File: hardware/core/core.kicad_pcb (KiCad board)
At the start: 2 copper layers, 256.5 x 129.5 mm, 86 parts, among them J1 9V_IN, J2 MIDI IN, J3 MIDI OUT 1, J4 MIDI OUT 2, J5 MIDI OUT 3, J6 MIDI OUT 4, J7 LCD, J8 USB_C_Receptacle_USB2.0_16P, SW1 FS, SW10 BOOT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

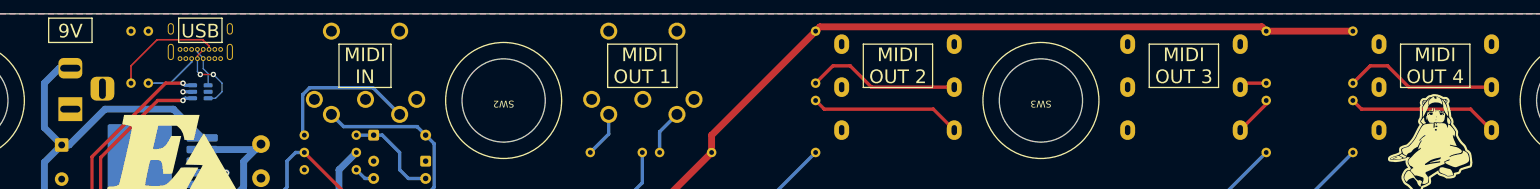
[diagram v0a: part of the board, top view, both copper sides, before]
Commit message: Adjust connector positions and reroute nearby traces
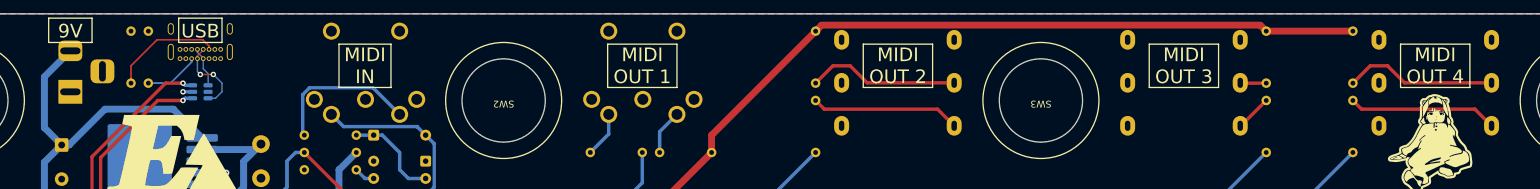
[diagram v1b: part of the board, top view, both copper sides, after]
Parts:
- moved J1 2.54 mm to (100.3, 99.1)
- moved J4 0.64 mm to (221.6, 97.7)
- moved J5 0.64 mm to (263.5, 97.7)
- moved J6 0.64 mm to (300.4, 97.7)
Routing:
- net +9V: track 50.9 -> 52.5 mm
- net Net-(J5-PadT): track 5.92 -> 5.35 mm
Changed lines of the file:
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@@
 	(footprint "Connector_BarrelJack:BarrelJack_Horizontal"
 		(layer "B.Cu")
-		(at 100.33 101.6 -90)
+		(at 100.33 99.06 -90)
 		(descr "DC Barrel Jack")
 		(tags "Power Jack")
@@
 	(footprint "midilord:CK635-006"
 		(layer "B.Cu")
-		(at 263.53 98.375 180)
+		(at 263.53 97.74 180)
 		(property "Reference" "J5"
 			(at 0 0.5 0)
@@
 	(footprint "midilord:CK635-006"
 		(layer "B.Cu")
-		(at 221.62 98.375 180)
+		(at 221.61 97.74 180)
 		(property "Reference" "J4"
 			(at 0 0.5 0)
@@
 	(footprint "midilord:CK635-006"
 		(layer "B.Cu")
-		(at 300.36 98.375 180)
+		(at 300.36 97.74 180)
 		(property "Reference" "J6"
 			(at 0 0.5 0)
@@
 	)
 	(segment
-		(start 100.33 95.6)
-		(end 98.71 95.6)
+		(start 96.52 104.312323)
+		(end 96.52 96.87)
 		(width 1)
 		(layer "B.Cu")
@@
 	)
 	(segment
-		(start 96.52 97.79)
+		(start 99.06 106.852323)
 		(end 96.52 104.312323)
 		(width 1)
@@
 	)
 	(segment
-		(start 96.52 104.312323)
-		(end 99.06 106.852323)
+		(start 105.41 101.6)
+		(end 100.157677 106.852323)
 		(width 1)
 		(layer "B.Cu")
@@
 	)
 	(segment
-		(start 105.41 101.6)
-		(end 100.157677 106.852323)
+		(start 96.52 96.87)
+		(end 100.33 93.06)
 		(width 1)
 		(layer "B.Cu")
@@
 	)
 	(segment
-		(start 98.71 95.6)
-		(end 96.52 97.79)
-		(width 1)
-		(layer "B.Cu")
-		(net 2)
-	)
-	(segment
 		(start 119.64 105.82)
 		(end 115.42 101.6)
@@
 	)
 	(segment
-		(start 272.365 97.79)
-		(end 271.78 98.375)
+		(start 271.83 97.79)
+		(end 271.78 97.74)
 		(width 0.5)
 		(layer "F.Cu")
@@
 	(segment
 		(start 275.59 97.79)
-		(end 272.365 97.79)
+		(end 271.83 97.79)
 		(width 0.5)
 		(layer "F.Cu")
@@
 	)
 	(segment
-		(start 275.59 100.865)
-		(end 271.78 104.675)
+		(start 275.59 100.33)
+		(end 271.88 104.04)
 		(width 0.5)
 		(layer "F.Cu")
@@
 	)
 	(segment
-		(start 275.59 100.33)
-		(end 275.59 100.865)
+		(start 271.88 104.04)
+		(end 271.78 104.04)
 		(width 0.5)
 		(layer "F.Cu")
@@
 	)
 	(segment
-		(start 288.29 97.79)
-		(end 290.83 95.25)
+		(start 293.37 95.25)
+		(end 295.86 97.74)
 		(width 0.5)
 		(layer "F.Cu")
@@
 	)
 	(segment
-		(start 296.495 98.375)
-		(end 308.61 98.375)
+		(start 288.29 97.79)
+		(end 290.83 95.25)
 		(width 0.5)
 		(layer "F.Cu")
@@
 	)
 	(segment
-		(start 293.37 95.25)
-		(end 296.495 98.375)
+		(start 295.86 97.74)
+		(end 308.61 97.74)
 		(width 0.5)
 		(layer "F.Cu")
@@
 	)
 	(segment
-		(start 288.29 100.33)
-		(end 289.56 101.6)
+		(start 289.56 101.6)
+		(end 306.17 101.6)
 		(width 0.5)
 		(layer "F.Cu")
@@
 	)
 	(segment
-		(start 289.56 101.6)
-		(end 305.535 101.6)
+		(start 306.17 101.6)
+		(end 308.61 104.04)
 		(width 0.5)
 		(layer "F.Cu")
@@
 	)
 	(segment
-		(start 305.535 101.6)
-		(end 308.61 104.675)
+		(start 288.29 100.33)
+		(end 289.56 101.6)
 		(width 0.5)
 		(layer "F.Cu")
@@
 	)
 	(segment
-		(start 146.05 120.65)
-		(end 142.24 124.46)
+		(start 210.431 89.289)
+		(end 209.55 90.17)
 		(width 1)
 		(layer "F.Cu")
@@
 	)
 	(segment
-		(start 209.55 90.17)
-		(end 194.31 105.41)
+		(start 146.05 120.65)
+		(end 142.24 124.46)
 		(width 1)
 		(layer "F.Cu")
@@
 	)
 	(segment
-		(start 210.185 89.535)
-		(end 209.55 90.17)
+		(start 209.55 90.17)
+		(end 194.31 105.41)
 		(width 1)
 		(layer "F.Cu")
@@
 	)
 	(segment
-		(start 274.955 89.535)
-		(end 210.185 89.535)
+		(start 146.05 120.65)
+		(end 181.61 120.65)
 		(width 1)
 		(layer "F.Cu")
@@
 	)
 	(segment
-		(start 146.05 120.65)
-		(end 181.61 120.65)
+		(start 274.709 89.289)
+		(end 210.431 89.289)
 		(width 1)
 		(layer "F.Cu")
@@
 	(segment
 		(start 275.59 90.17)
-		(end 274.955 89.535)
+		(end 274.709 89.289)
 		(width 1)
 		(layer "F.Cu")
@@
 	)
 	(segment
-		(start 209.55 100.33)
-		(end 210.82 101.6)
+		(start 227.42 101.6)
+		(end 229.86 104.04)
 		(width 0.5)
 		(layer "F.Cu")
@@
 	)
 	(segment
-		(start 210.82 101.6)
-		(end 226.795 101.6)
+		(start 209.55 100.33)
+		(end 210.82 101.6)
 		(width 0.5)
 		(layer "F.Cu")
@@
 	)
 	(segment
-		(start 226.795 101.6)
-		(end 229.87 104.675)
+		(start 210.82 101.6)
+		(end 227.42 101.6)
 		(width 0.5)
 		(layer "F.Cu")
@@
 	)
 	(segment
-		(start 217.755 98.375)
-		(end 229.87 98.375)
+		(start 212.09 95.25)
+		(end 214.63 95.25)
 		(width 0.5)
 		(layer "F.Cu")
@@
 	)
 	(segment
-		(start 209.55 97.79)
-		(end 212.09 95.25)
+		(start 214.63 95.25)
+		(end 217.12 97.74)
 		(width 0.5)
 		(layer "F.Cu")
@@
 	)
 	(segment
-		(start 214.63 95.25)
-		(end 217.755 98.375)
+		(start 209.55 97.79)
+		(end 212.09 95.25)
 		(width 0.5)
 		(layer "F.Cu")
@@
 	)
 	(segment
-		(start 212.09 95.25)
-		(end 214.63 95.25)
+		(start 217.12 97.74)
+		(end 229.86 97.74)
 		(width 0.5)
 		(layer "F.Cu")

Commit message: Move footswitch silkscreen circle to Dwgs.User layer
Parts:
- removed the G*** at (300.4, 106.7)
- moved G*** 117.8 mm to (203.2, 189.2)
- moved J1 0.64 mm to (100.3, 98.4)
- moved J2 0.18 mm to (143.5, 95.2)
- moved J3 0.18 mm to (184.2, 95.2)
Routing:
- net +9V: track 52.5 -> 53.1 mm
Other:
- board text added: "midiLORD"
- board text removed: "midilord"

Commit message: Add event system, switch matrix, MIDI outputs, and LED helpers
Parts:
- removed the G*** at (123.9, 204.3)
- removed J6: MIDI OUT 4, midilord:CK635-006
- added D19: 1N4148, Diode_THT:D_T-1_P5.08mm_Horizontal, B.Cu at (310.5, 140.3)
- added D20: 1N4148, Diode_THT:D_T-1_P5.08mm_Horizontal, B.Cu at (302.3, 140.3)
- added J9: MIDI OUT 2/3, midilord:CK635-037, B.Cu at (254.6, 97.8)
- added JP9: CONTRAST, Jumper:SolderJumper-3_P1.3mm_Open_RoundedPad1.0x1.5mm, F.Cu at (97.1, 167.6)
- added K1: G5V-1, Relay_THT:Relay_SPDT_Omron_G5V-1, B.Cu at (310.5, 137.2)
- added K2: G5V-1, Relay_THT:Relay_SPDT_Omron_G5V-1, B.Cu at (302.3, 137.2)
- added Q1: 2N3906, Package_TO_SOT_THT:TO-92_Inline_Wide, B.Cu at (217.2, 109.9)
- added Q2: 2N3906, Package_TO_SOT_THT:TO-92_Inline_Wide, B.Cu at (252.1, 115.6)
- added Q3: 2N3904, Package_TO_SOT_THT:TO-92_Inline_Wide, B.Cu at (310.5, 144.1)
- added Q4: 2N3904, Package_TO_SOT_THT:TO-92_Inline_Wide, B.Cu at (302.3, 144.1)
- added R17: 4.7K, Resistor_THT:R_Axial_DIN0204_L3.6mm_D1.6mm_P7.62mm_Horizontal, B.Cu at (205.7, 108.6)
- added R18: 4.7K, Resistor_THT:R_Axial_DIN0204_L3.6mm_D1.6mm_P7.62mm_Horizontal, B.Cu at (250.8, 120.7)
- D11, D12, D13, D14, D15, D16, D17, D18: footprint Diode_THT:D_DO-35_SOD27_P7.62mm_Horizontal -> Diode_THT:D_T-1_P5.08mm_Horizontal
- J4: value MIDI OUT 2 -> SWITCHES OUT; footprint midilord:CK635-006 -> midilord:CK635-037
- J5: value MIDI OUT 3 -> EXP/AUX IN; footprint midilord:CK635-006 -> midilord:CK635-037
- R10: value 33R -> 4.7K
- R3, R5, R7: value 10R -> 220R
- R4, R6, R8: value 33R -> 220R
- R9: value 10R -> 4.7K
- moved D10 234.5 mm to (306.1, 186.7), turned to 180 degrees
- moved D7 228.3 mm to (100.3, 186.7), turned to 180 degrees
- moved C15 223.4 mm to (293.4, 182.9)
- moved C12 205.1 mm to (113.0, 183.0), turned to -90 degrees
- moved D9 103.0 mm to (237.5, 186.7), turned to 180 degrees
- moved D8 98.3 mm to (168.9, 186.7), turned to 180 degrees
- moved C13 77.2 mm to (181.6, 183.0), turned to -90 degrees
- moved C14 77.2 mm to (224.8, 182.9), turned to -90 degrees
- moved D6 71.0 mm to (306.1, 118.1)
- moved D3 69.6 mm to (100.3, 118.1)
- moved D5 69.1 mm to (237.5, 118.1)
- moved D4 68.6 mm to (168.9, 118.1)
- moved U3 68.1 mm to (134.6, 204.5), turned to 0 degrees
- moved J4 67.3 mm to (288.9, 97.8)
- moved C11 66.7 mm to (293.4, 121.8)
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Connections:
- J7 pad 16: unconnected-(J7-Pin_16-Pad16) -> Net-(J7-Pin_16)
- R10 pad 1: MIDI_OUT4 -> SW_OUT2
- R3 pad 1: +3.3V -> +5V
- R4 pad 1: MIDI_OUT1 -> Net-(Q1-E)
- R5 pad 1: +3.3V -> +5V
- R5 pad 2: Net-(J4-PadR) -> Net-(J9-2R)
- R6 pad 1: MIDI_OUT2 -> Net-(Q2-E)
- R6 pad 2: Net-(J4-PadT) -> Net-(J9-T)
- R7 pad 1: +3.3V -> Net-(J9-R)
- R7 pad 2: Net-(J5-PadR) -> +5V
- R8 pad 1: MIDI_OUT3 -> Net-(Q2-E)
- R8 pad 2: Net-(J5-PadT) -> Net-(J9-2T)
- R9 pad 1: +3.3V -> SW_OUT1
- RV1 pad 3: GND -> Net-(JP9-C)
- U3 pad 10: DB6 -> RS
- U3 pad 11: DB5 -> E2
- U3 pad 12: DB4 -> SW_OUT3
- U3 pad 17: unconnected-(U3-IO9-Pad17) -> MIDI_IN
- U3 pad 18: unconnected-(U3-IO10-Pad18) -> MIDI_OUT1
- U3 pad 19: unconnected-(U3-IO11-Pad19) -> MIDI_OUT2
- U3 pad 22: MIDI_IN -> EXP1
- U3 pad 23: MIDI_OUT1 -> EXP2
- U3 pad 24: MIDI_OUT2 -> SW_OUT1
- U3 pad 25: MIDI_OUT3 -> SW_OUT2
- U3 pad 26: MIDI_OUT4 -> unconnected-(U3-IO45-Pad26)
- U3 pad 31: MCU_LED -> SW_OUT4
- U3 pad 32: C4 -> C1
- U3 pad 33: C3 -> C2
- U3 pad 34: C2 -> C3
- U3 pad 35: C1 -> C4
- U3 pad 4: unconnected-(U3-IO4-Pad4) -> MCU_LED
- U3 pad 5: unconnected-(U3-IO5-Pad5) -> DB7
- U3 pad 6: E1 -> DB6
- U3 pad 7: RS -> DB5
- U3 pad 8: E2 -> DB4
- U3 pad 9: DB7 -> E1
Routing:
- net MIDI_OUT4: track 239.7 -> 0.00 mm
- net MIDI_IN: track 100.8 -> 332.2 mm
- net MIDI_OUT3: track 227.5 -> 0.00 mm
- net SW_OUT1: track 0.00 -> 224.0 mm, vias 0 -> 1
- net SW_OUT2: track 0.00 -> 221.8 mm, vias 0 -> 1
- net R1: track 274.6 -> 475.7 mm, vias 4 -> 2
- net Net-(D6-DOUT): track 72.8 -> 273.4 mm
- net MIDI_OUT1: track 138.2 -> 308.7 mm
- net MIDI_OUT2: track 161.2 -> 258.9 mm
- net +3.3V: track 293.7 -> 208.9 mm
- net MCU_LED: track 32.8 -> 117.1 mm, vias 1 -> 0
- net Net-(R14-Pad1): track 52.2 -> 132.2 mm, vias 3 -> 0
- net Net-(R13-Pad1): track 50.7 -> 129.0 mm, vias 3 -> 0
- net DB4: track 14.0 -> 76.8 mm
- net DB5: track 21.3 -> 81.3 mm
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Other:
- board size 256.5 x 129.5 mm -> 228.6 x 129.5 mm
- board text added: "EXP/AUX IN"
- board text added: "MIDI OUT 2/3"
- board text added: "SWITCHES OUT"
- board text added: "V C G"
- board text removed: "MIDI OUT 2"
- board text removed: "MIDI OUT 3"
- board text removed: "MIDI OUT 4"

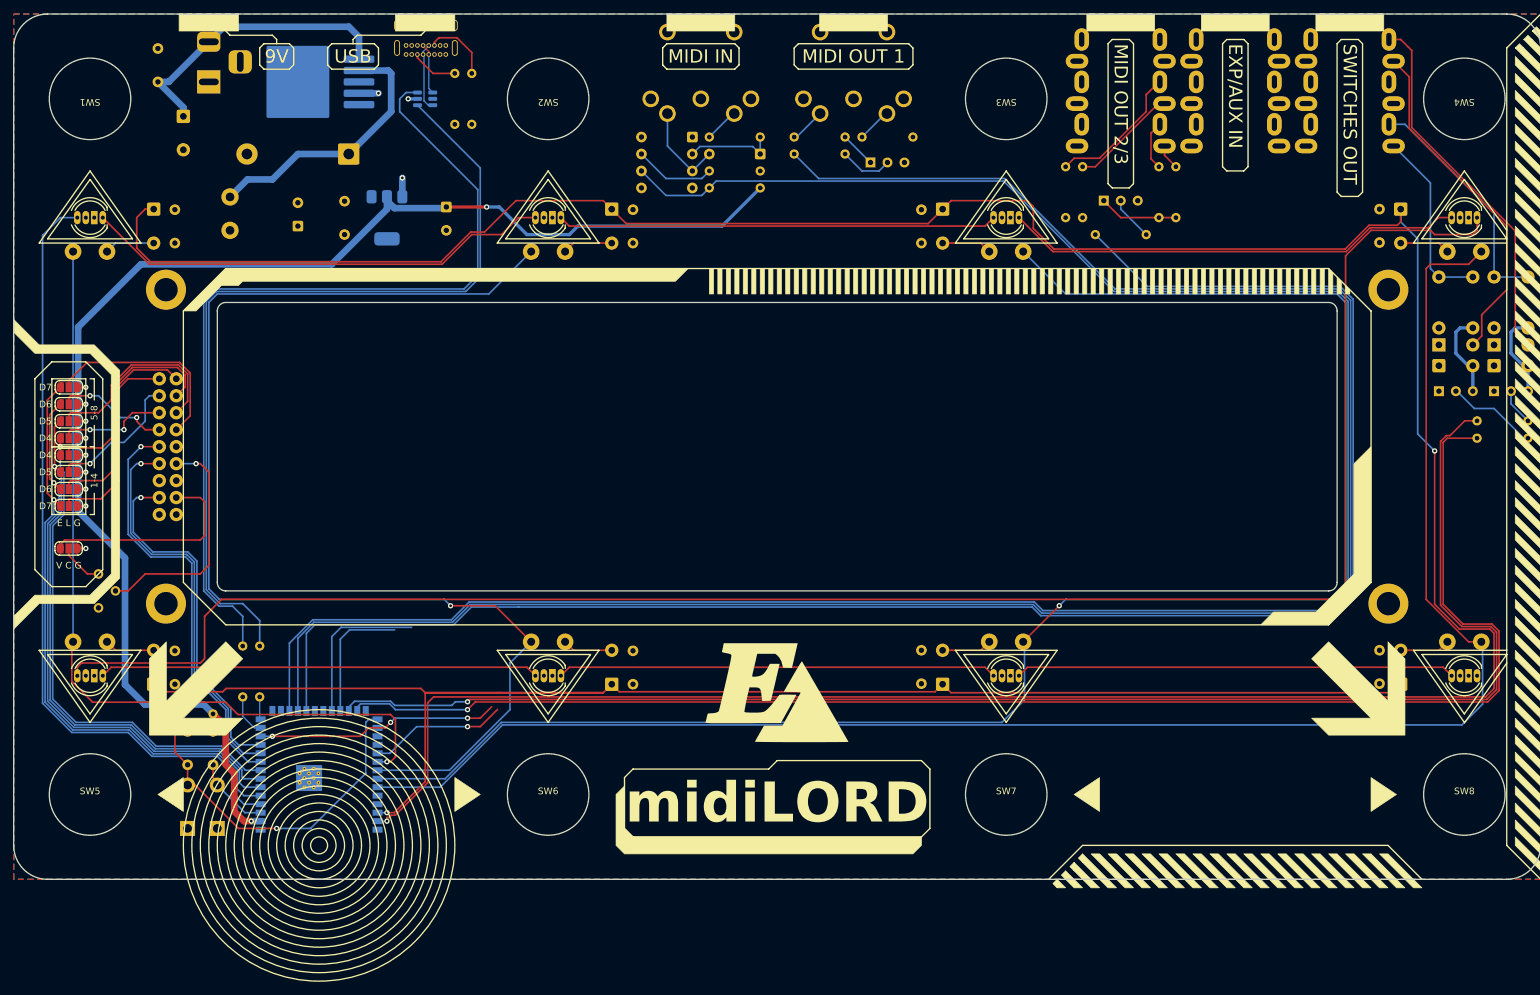
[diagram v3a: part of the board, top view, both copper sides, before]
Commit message: Replace footswitch connector nets with aux/expression nets and renumber
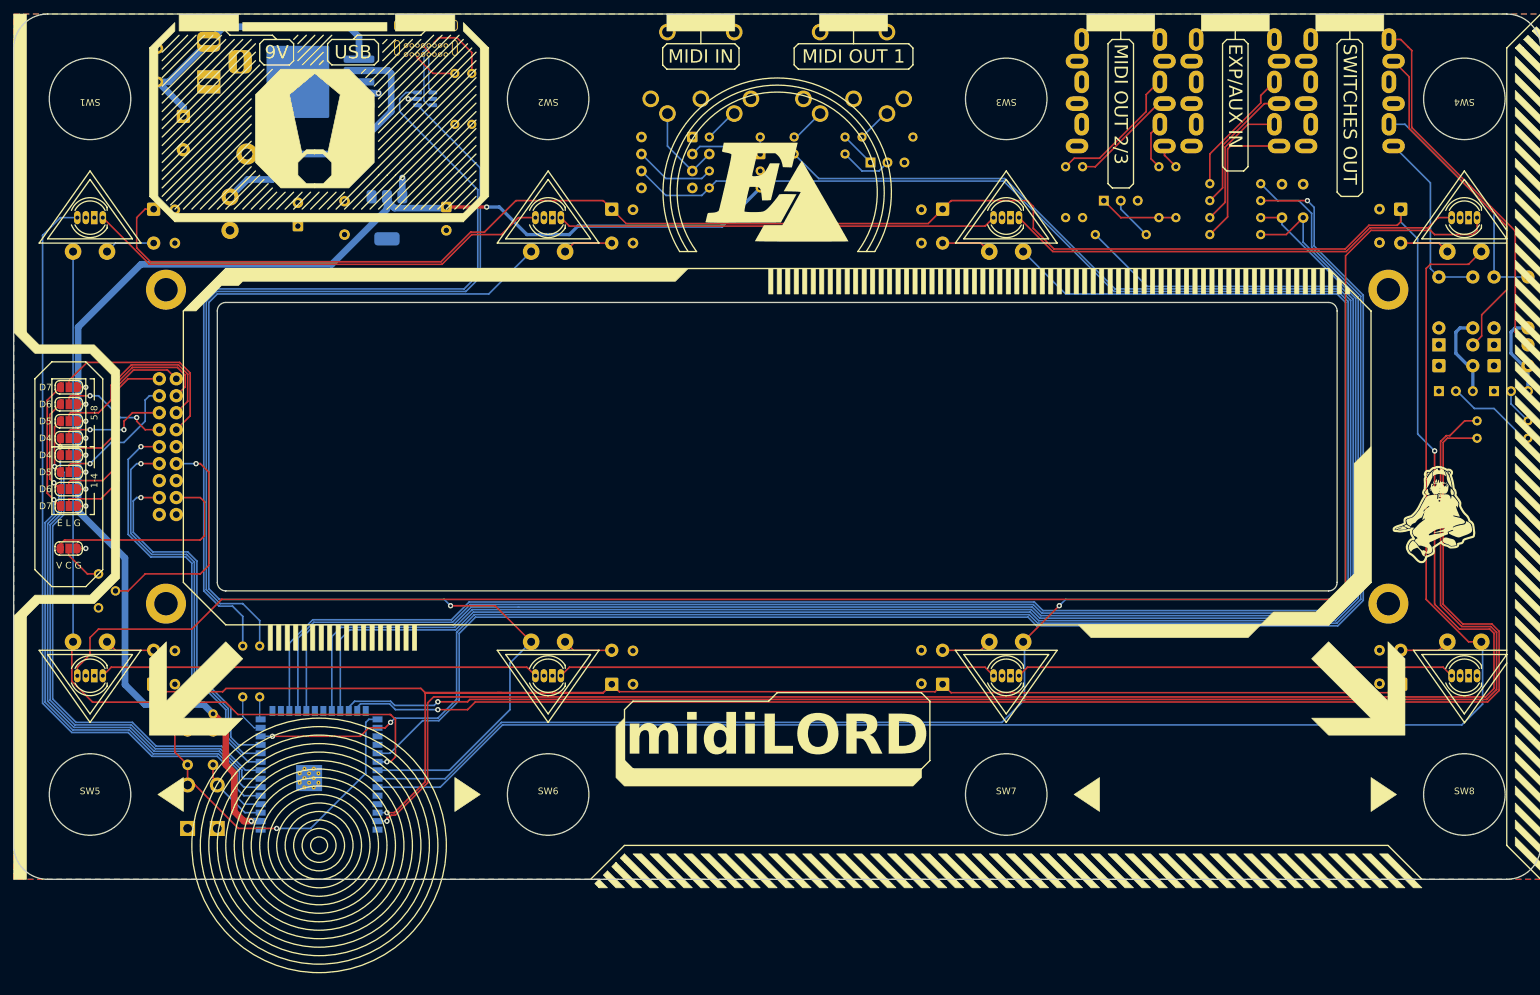
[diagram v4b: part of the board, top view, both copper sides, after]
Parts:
- added C16: 10n, Capacitor_THT:C_Rect_L7.0mm_W2.5mm_P5.00mm, B.Cu at (278.8, 118.1)
- added C17: 10n, Capacitor_THT:C_Rect_L7.0mm_W2.5mm_P5.00mm, B.Cu at (281.9, 118.1)
- added G***: LOGO, midilord:lain, F.Cu at (302.3, 162.6)
- added R19: 2.2K, Resistor_THT:R_Axial_DIN0204_L3.6mm_D1.6mm_P7.62mm_Horizontal, B.Cu at (275.6, 115.6)
- added R20: 2.2K, Resistor_THT:R_Axial_DIN0204_L3.6mm_D1.6mm_P7.62mm_Horizontal, B.Cu at (275.6, 120.7)
- added R21: 2.2K, Resistor_THT:R_Axial_DIN0204_L3.6mm_D1.6mm_P7.62mm_Horizontal, B.Cu at (275.6, 113.0)
- added R22: 2.2K, Resistor_THT:R_Axial_DIN0204_L3.6mm_D1.6mm_P7.62mm_Horizontal, B.Cu at (275.6, 118.1)
- moved G*** 74.9 mm to (203.2, 114.3)
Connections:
- J5 pad 1: unconnected-(J5-S-Pad1) -> GND
- J5 pad 2: unconnected-(J5-2S-Pad2) -> GND
- J5 pad 3: unconnected-(J5-R-Pad3) -> Net-(J5-R)
- J5 pad 4: unconnected-(J5-2R-Pad4) -> Net-(J5-2R)
- J5 pad 5: unconnected-(J5-T-Pad5) -> Net-(J5-T)
- J5 pad 6: unconnected-(J5-2T-Pad6) -> Net-(J5-2T)
- U3 pad 12: SW_OUT3 -> AUX1
- U3 pad 31: SW_OUT4 -> AUX2
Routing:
- net AUX1: track 0.00 -> 250.4 mm, vias 0 -> 2
- net AUX2: track 0.00 -> 234.3 mm, vias 0 -> 1
- net EXP2: track 19.5 -> 234.5 mm
- net EXP1: track 23.7 -> 232.5 mm
- net SW_OUT3: track 36.4 -> 0.00 mm, vias 3 -> 0
- net Net-(J5-2T): track 0.00 -> 21.8 mm
- net SW_OUT4: track 20.7 -> 0.00 mm, vias 1 -> 0
- net Net-(J5-T): track 0.00 -> 20.3 mm
- net Net-(J5-2R): track 0.00 -> 20.1 mm
- net Net-(J5-R): track 0.00 -> 19.2 mm
- net Net-(D6-DOUT): track 273.4 -> 271.2 mm
